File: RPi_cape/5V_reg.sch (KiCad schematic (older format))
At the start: 18 parts, among them U34 LMZ14203

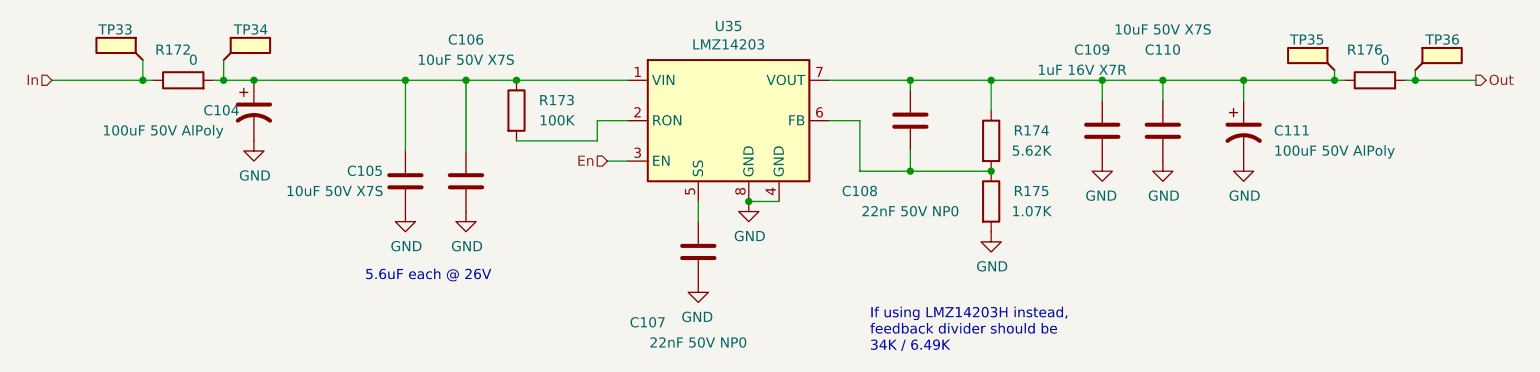
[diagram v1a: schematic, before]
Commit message: Updates based on testing, extra documentation
Added thermal calculations, possible thermal-induced problems to fault-condition list
Renamed error calculations file
Added some bringup tests
Changed 24V LED resistors (R20, R22) to 24.9K to consolidate BOM
Adjusted audio amp volume and filtering according to breadboard experiments
Moved bottom-end mounting holes and encoder connectors to avoid interfering mechanically with Raspberry Pi
Replaced under-sized power-ORing diodes with better Schottky option, added heatsinking with copper planes
Improved LMZ14203 heatsinking by removing thermal reliefs, re-arranging input-current-measurement testpoints to increase top-layer copper area
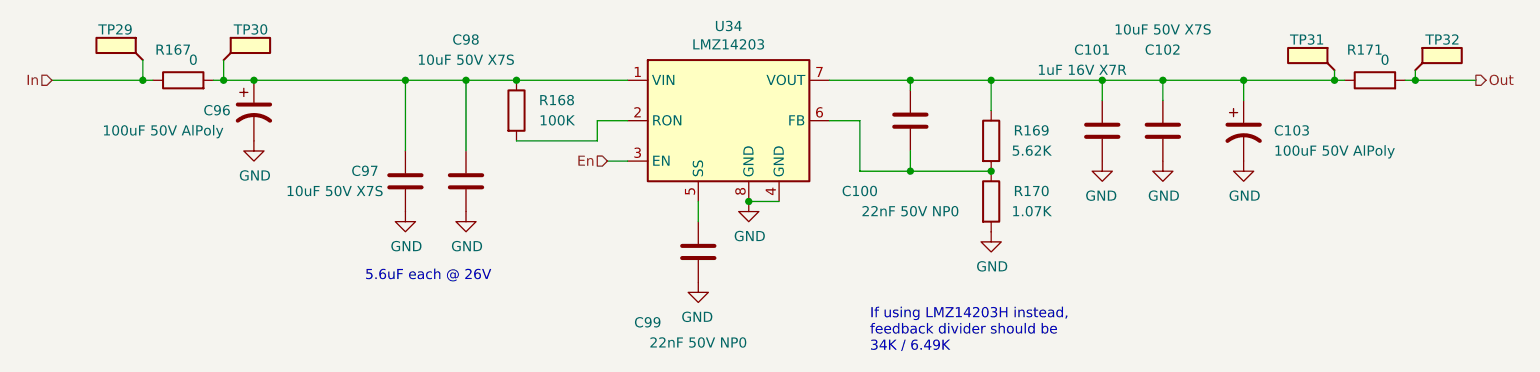
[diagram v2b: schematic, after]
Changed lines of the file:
@@
 $Descr A4 11693 8268
 encoding utf-8
-Sheet 11 15
+Sheet 10 15
 Title "Raspberry Pi Hat for JamVent Adaptation"
 Date ""
-Rev "1.8"
+Rev "1.9"
 Comp "US JamVent Team"
 Comment1 "Don Straney"
@@
 AR Path="/5EE065CD/5EE088D9" Ref="U34"  Part="1"
 AR Path="/5EEB3F52/5EE088D9" Ref="U35"  Part="1"
-F 0 "U35" H 5000 3417 50  0000 C CNN
+F 0 "U34" H 5000 3417 50  0000 C CNN
 F 1 "LMZ14203" H 5000 3326 50  0000 C CNN
 F 2 "Ventilator:TI_TO-PMOD-7" H 5000 2100 50  0001 C CNN
@@
 AR Path="/5EE065CD/5EE14EEB" Ref="R169"  Part="1"
 AR Path="/5EEB3F52/5EE14EEB" Ref="R174"  Part="1"
-F 0 "R174" H 6500 3100 50  0000 C CNN
+F 0 "R169" H 6500 3100 50  0000 C CNN
 F 1 "5.62K" H 6500 3000 50  0000 C CNN
 F 2 "Resistor_SMD:R_1206_3216Metric" V 6230 3050 50  0001 C CNN
@@
 AR Path="/5EE065CD/5EE14EF1" Ref="C97"  Part="1"
 AR Path="/5EEB3F52/5EE14EF1" Ref="C105"  Part="1"
-F 0 "C105" H 3600 3300 50  0000 C CNN
+F 0 "C97" H 3600 3300 50  0000 C CNN
 F 1 "10uF 50V X7S" H 3750 3200 50  0000 C CNN
 F 2 "Capacitor_SMD:C_1210_3225Metric" H 3438 3100 50  0001 C CNN
@@
 AR Path="/5EE065CD/5EE16CD0" Ref="R170"  Part="1"
 AR Path="/5EEB3F52/5EE16CD0" Ref="R175"  Part="1"
-F 0 "R175" H 6500 3400 50  0000 C CNN
+F 0 "R170" H 6500 3400 50  0000 C CNN
 F 1 "1.07K" H 6500 3300 50  0000 C CNN
 F 2 "Resistor_SMD:R_1206_3216Metric" V 6230 3350 50  0001 C CNN
@@
 AR Path="/5EE065CD/5EE170F2" Ref="R168"  Part="1"
 AR Path="/5EEB3F52/5EE170F2" Ref="R173"  Part="1"
-F 0 "R173" H 4150 2950 50  0000 C CNN
+F 0 "R168" H 4150 2950 50  0000 C CNN
 F 1 "100K" H 4150 2850 50  0000 C CNN
 F 2 "Resistor_SMD:R_1206_3216Metric" V 3880 2900 50  0001 C CNN
@@
 AR Path="/5EE065CD/5EE1CE10" Ref="#PWR0301"  Part="1"
 AR Path="/5EEB3F52/5EE1CE10" Ref="#PWR0310"  Part="1"
-F 0 "#PWR0310" H 3400 3150 50  0001 C CNN
+F 0 "#PWR0301" H 3400 3150 50  0001 C CNN
 F 1 "GND" H 3405 3227 50  0000 C CNN
 F 2 "" H 3400 3400 50  0001 C CNN
@@
 AR Path="/5EE065CD/5EE1D159" Ref="#PWR0304"  Part="1"
 AR Path="/5EEB3F52/5EE1D159" Ref="#PWR0313"  Part="1"
-F 0 "#PWR0313" H 5100 3100 50  0001 C CNN
+F 0 "#PWR0304" H 5100 3100 50  0001 C CNN
 F 1 "GND" H 5105 3177 50  0000 C CNN
 F 2 "" H 5100 3350 50  0001 C CNN
@@
 AR Path="/5EE065CD/5EE1E75C" Ref="#PWR0305"  Part="1"
 AR Path="/5EEB3F52/5EE1E75C" Ref="#PWR0314"  Part="1"
-F 0 "#PWR0314" H 6300 3250 50  0001 C CNN
+F 0 "#PWR0305" H 6300 3250 50  0001 C CNN
 F 1 "GND" H 6305 3327 50  0000 C CNN
 F 2 "" H 6300 3500 50  0001 C CNN
@@
 AR Path="/5EE065CD/5EE2670E" Ref="C99"  Part="1"
 AR Path="/5EEB3F52/5EE2670E" Ref="C107"  Part="1"
-F 0 "C107" H 4600 3950 50  0000 C CNN
+F 0 "C99" H 4600 3950 50  0000 C CNN
 F 1 "22nF 50V NP0" H 4850 4050 50  0000 C CNN
 F 2 "Capacitor_SMD:C_0805_2012Metric" H 4888 3450 50  0001 C CNN
@@
 AR Path="/5EE065CD/5EE26714" Ref="#PWR0303"  Part="1"
 AR Path="/5EEB3F52/5EE26714" Ref="#PWR0312"  Part="1"
-F 0 "#PWR0312" H 4850 3500 50  0001 C CNN
+F 0 "#PWR0303" H 4850 3500 50  0001 C CNN
 F 1 "GND" H 4855 3577 50  0000 C CNN
 F 2 "" H 4850 3750 50  0001 C CNN
@@
 AR Path="/5EE065CD/5EE27BE3" Ref="C100"  Part="1"
 AR Path="/5EEB3F52/5EE27BE3" Ref="C108"  Part="1"
-F 0 "C108" H 5650 3300 50  0000 C CNN
+F 0 "C100" H 5650 3300 50  0000 C CNN
 F 1 "22nF 50V NP0" H 5900 3400 50  0000 C CNN
 F 2 "Capacitor_SMD:C_0805_2012Metric" H 5938 2800 50  0001 C CNN
@@
 AR Path="/5EE065CD/5EE2ABB7" Ref="C102"  Part="1"
 AR Path="/5EEB3F52/5EE2ABB7" Ref="C110"  Part="1"
-F 0 "C110" H 7150 3400 50  0000 C CNN
+F 0 "C102" H 7150 3400 50  0000 C CNN
 F 1 "10uF 50V X7S" H 7150 3500 50  0000 C CNN
 F 2 "Capacitor_SMD:C_1210_3225Metric" H 7188 2850 50  0001 C CNN
@@
 AR Path="/5EE065CD/5EE2ABBD" Ref="#PWR0307"  Part="1"
 AR Path="/5EEB3F52/5EE2ABBD" Ref="#PWR0316"  Part="1"
-F 0 "#PWR0316" H 7150 2900 50  0001 C CNN
+F 0 "#PWR0307" H 7150 2900 50  0001 C CNN
 F 1 "GND" H 7155 2977 50  0000 C CNN
 F 2 "" H 7150 3150 50  0001 C CNN
@@
 AR Path="/5EE065CD/5EE35666" Ref="C96"  Part="1"
 AR Path="/5EEB3F52/5EE35666" Ref="C104"  Part="1"
-F 0 "C104" H 2400 2900 50  0000 L CNN
+F 0 "C96" H 2400 2900 50  0000 L CNN
 F 1 "100uF 50V AlPoly" H 1900 2800 50  0000 L CNN
 F 2 "Capacitor_SMD:CP_Elec_10x10.5" H 2650 2900 50  0001 C CNN
@@
 AR Path="/5EE065CD/5EE3566C" Ref="#PWR0300"  Part="1"
 AR Path="/5EEB3F52/5EE3566C" Ref="#PWR0309"  Part="1"
-F 0 "#PWR0309" H 2650 2800 50  0001 C CNN
+F 0 "#PWR0300" H 2650 2800 50  0001 C CNN
 F 1 "GND" H 2655 2877 50  0000 C CNN
 F 2 "" H 2650 3050 50  0001 C CNN
@@
 AR Path="/5EE065CD/5EE38A1F" Ref="C103"  Part="1"
 AR Path="/5EEB3F52/5EE38A1F" Ref="C111"  Part="1"
-F 0 "C111" H 7700 3000 50  0000 L CNN
+F 0 "C103" H 7700 3000 50  0000 L CNN
 F 1 "100uF 50V AlPoly" H 7700 2900 50  0000 L CNN
 F 2 "Capacitor_SMD:CP_Elec_10x10.5" H 7550 3000 50  0001 C CNN
@@
 AR Path="/5EE065CD/5EE38A25" Ref="#PWR0308"  Part="1"
 AR Path="/5EEB3F52/5EE38A25" Ref="#PWR0317"  Part="1"
-F 0 "#PWR0317" H 7550 2900 50  0001 C CNN
+F 0 "#PWR0308" H 7550 2900 50  0001 C CNN
 F 1 "GND" H 7555 2977 50  0000 C CNN
 F 2 "" H 7550 3150 50  0001 C CNN
@@
 AR Path="/5EE065CD/5EE41F5A" Ref="#PWR0306"  Part="1"
 AR Path="/5EEB3F52/5EE41F5A" Ref="#PWR0315"  Part="1"
-F 0 "#PWR0315" H 6850 2900 50  0001 C CNN
+F 0 "#PWR0306" H 6850 2900 50  0001 C CNN
 F 1 "GND" H 6855 2977 50  0000 C CNN
 F 2 "" H 6850 3150 50  0001 C CNN
@@
 AR Path="/5EE065CD/5EE41F60" Ref="C101"  Part="1"
 AR Path="/5EEB3F52/5EE41F60" Ref="C109"  Part="1"
-F 0 "C109" H 6800 2600 50  0000 C CNN
+F 0 "C101" H 6800 2600 50  0000 C CNN
 F 1 "1uF 16V X7R" H 6750 2700 50  0000 C CNN
 F 2 "Capacitor_SMD:C_0805_2012Metric" H 6888 2850 50  0001 C CNN
@@
 AR Path="/5EE065CD/5EE4C23D" Ref="R171"  Part="1"
 AR Path="/5EEB3F52/5EE4C23D" Ref="R176"  Part="1"
-F 0 "R176" V 8350 2800 50  0000 C CNN
+F 0 "R171" V 8350 2800 50  0000 C CNN
 F 1 "0" V 8300 2700 50  0000 C CNN
 F 2 "Resistor_SMD:R_1206_3216Metric" V 8130 2750 50  0001 C CNN
@@
 AR Path="/5EE065CD/5EE50890" Ref="R167"  Part="1"
 AR Path="/5EEB3F52/5EE50890" Ref="R172"  Part="1"
-F 0 "R172" V 2450 2800 50  0000 C CNN
+F 0 "R167" V 2450 2800 50  0000 C CNN
 F 1 "0" V 2400 2700 50  0000 C CNN
 F 2 "Resistor_SMD:R_1206_3216Metric" V 2230 2750 50  0001 C CNN
@@
 AR Path="/5EE065CD/5EEA6827" Ref="TP30"  Part="1"
 AR Path="/5EEB3F52/5EEA6827" Ref="TP34"  Part="1"
-F 0 "TP34" H 2550 2800 50  0000 L CNN
+F 0 "TP30" H 2550 2800 50  0000 L CNN
 F 1 "TestPoint_Flag" H 2760 2653 50  0001 L CNN
 F 2 "TestPoint:TestPoint_Keystone_5019_Minature" H 2700 2650 50  0001 C CNN
@@
 AR Path="/5EE065CD/5EEA7A58" Ref="TP29"  Part="1"
 AR Path="/5EEB3F52/5EEA7A58" Ref="TP33"  Part="1"
-F 0 "TP33" H 2150 2800 50  0000 L CNN
+F 0 "TP29" H 2150 2800 50  0000 L CNN
 F 1 "TestPoint_Flag" H 2360 2653 50  0001 L CNN
 F 2 "TestPoint:TestPoint_Keystone_5019_Minature" H 2300 2650 50  0001 C CNN
@@
 AR Path="/5EE065CD/5EEA8BCB" Ref="TP31"  Part="1"
 AR Path="/5EEB3F52/5EEA8BCB" Ref="TP35"  Part="1"
-F 0 "TP35" H 8050 2850 50  0000 L CNN
+F 0 "TP31" H 8050 2850 50  0000 L CNN
 F 1 "TestPoint_Flag" H 8260 2703 50  0001 L CNN
 F 2 "TestPoint:TestPoint_Keystone_5019_Minature" H 8200 2700 50  0001 C CNN
@@
 AR Path="/5EE065CD/5EEAED2A" Ref="TP32"  Part="1"
 AR Path="/5EEB3F52/5EEAED2A" Ref="TP36"  Part="1"
-F 0 "TP36" H 8450 2850 50  0000 L CNN
+F 0 "TP32" H 8450 2850 50  0000 L CNN
 F 1 "TestPoint_Flag" H 8660 2703 50  0001 L CNN
 F 2 "TestPoint:TestPoint_Keystone_5019_Minature" H 8600 2700 50  0001 C CNN
@@
 AR Path="/5EE065CD/5F025002" Ref="C98"  Part="1"
 AR Path="/5EEB3F52/5F025002" Ref="C106"  Part="1"
-F 0 "C106" H 3700 3950 50  0000 C CNN
+F 0 "C98" H 3700 3950 50  0000 C CNN
 F 1 "10uF 50V X7S" H 3700 3850 50  0000 C CNN
 F 2 "Capacitor_SMD:C_1210_3225Metric" H 3738 3100 50  0001 C CNN
@@
 AR Path="/5EE065CD/5F025009" Ref="#PWR0302"  Part="1"
 AR Path="/5EEB3F52/5F025009" Ref="#PWR0311"  Part="1"
-F 0 "#PWR0311" H 3700 3150 50  0001 C CNN
+F 0 "#PWR0302" H 3700 3150 50  0001 C CNN
 F 1 "GND" H 3705 3227 50  0000 C CNN
 F 2 "" H 3700 3400 50  0001 C CNN

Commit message: Cleanup, manufacturing
Added doc on differences between 'proto' version and 'full' version
Added manufacturing README in proto version
Removed unused hardwired-limited O2 alarm nets in proto version
Fixed missed-annotation on D1 in full version
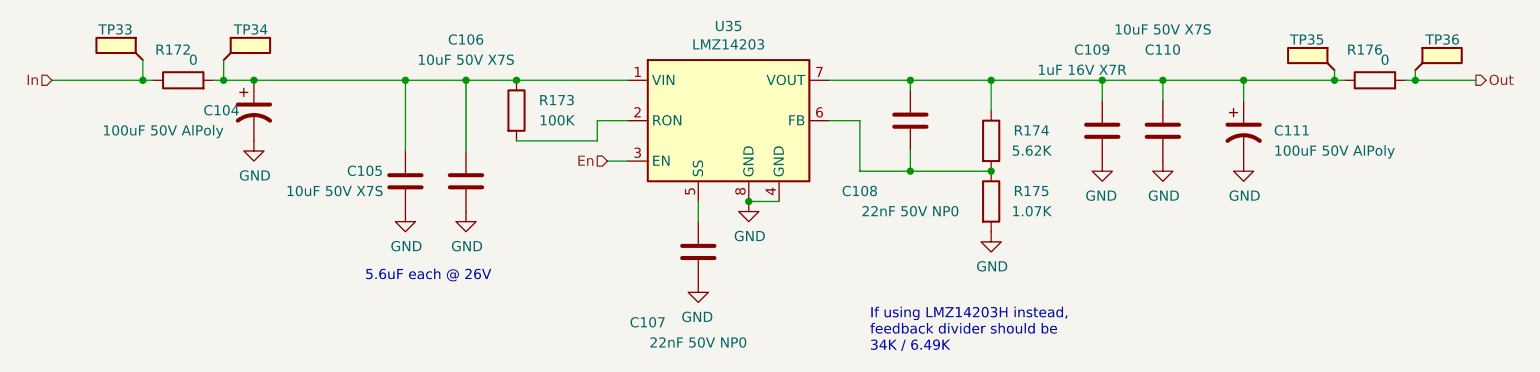
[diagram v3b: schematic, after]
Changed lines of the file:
@@
 $Descr A4 11693 8268
 encoding utf-8
-Sheet 10 15
+Sheet 11 15
 Title "Raspberry Pi Hat for JamVent Adaptation"
 Date ""
@@
 AR Path="/5EE065CD/5EE088D9" Ref="U34"  Part="1"
 AR Path="/5EEB3F52/5EE088D9" Ref="U35"  Part="1"
-F 0 "U34" H 5000 3417 50  0000 C CNN
+F 0 "U35" H 5000 3417 50  0000 C CNN
 F 1 "LMZ14203" H 5000 3326 50  0000 C CNN
 F 2 "Ventilator:TI_TO-PMOD-7" H 5000 2100 50  0001 C CNN
@@
 AR Path="/5EE065CD/5EE14EEB" Ref="R169"  Part="1"
 AR Path="/5EEB3F52/5EE14EEB" Ref="R174"  Part="1"
-F 0 "R169" H 6500 3100 50  0000 C CNN
+F 0 "R174" H 6500 3100 50  0000 C CNN
 F 1 "5.62K" H 6500 3000 50  0000 C CNN
 F 2 "Resistor_SMD:R_1206_3216Metric" V 6230 3050 50  0001 C CNN
@@
 AR Path="/5EE065CD/5EE14EF1" Ref="C97"  Part="1"
 AR Path="/5EEB3F52/5EE14EF1" Ref="C105"  Part="1"
-F 0 "C97" H 3600 3300 50  0000 C CNN
+F 0 "C105" H 3600 3300 50  0000 C CNN
 F 1 "10uF 50V X7S" H 3750 3200 50  0000 C CNN
 F 2 "Capacitor_SMD:C_1210_3225Metric" H 3438 3100 50  0001 C CNN
@@
 AR Path="/5EE065CD/5EE16CD0" Ref="R170"  Part="1"
 AR Path="/5EEB3F52/5EE16CD0" Ref="R175"  Part="1"
-F 0 "R170" H 6500 3400 50  0000 C CNN
+F 0 "R175" H 6500 3400 50  0000 C CNN
 F 1 "1.07K" H 6500 3300 50  0000 C CNN
 F 2 "Resistor_SMD:R_1206_3216Metric" V 6230 3350 50  0001 C CNN
@@
 AR Path="/5EE065CD/5EE170F2" Ref="R168"  Part="1"
 AR Path="/5EEB3F52/5EE170F2" Ref="R173"  Part="1"
-F 0 "R168" H 4150 2950 50  0000 C CNN
+F 0 "R173" H 4150 2950 50  0000 C CNN
 F 1 "100K" H 4150 2850 50  0000 C CNN
 F 2 "Resistor_SMD:R_1206_3216Metric" V 3880 2900 50  0001 C CNN
@@
 AR Path="/5EE065CD/5EE1CE10" Ref="#PWR0301"  Part="1"
 AR Path="/5EEB3F52/5EE1CE10" Ref="#PWR0310"  Part="1"
-F 0 "#PWR0301" H 3400 3150 50  0001 C CNN
+F 0 "#PWR0310" H 3400 3150 50  0001 C CNN
 F 1 "GND" H 3405 3227 50  0000 C CNN
 F 2 "" H 3400 3400 50  0001 C CNN
@@
 AR Path="/5EE065CD/5EE1D159" Ref="#PWR0304"  Part="1"
 AR Path="/5EEB3F52/5EE1D159" Ref="#PWR0313"  Part="1"
-F 0 "#PWR0304" H 5100 3100 50  0001 C CNN
+F 0 "#PWR0313" H 5100 3100 50  0001 C CNN
 F 1 "GND" H 5105 3177 50  0000 C CNN
 F 2 "" H 5100 3350 50  0001 C CNN
@@
 AR Path="/5EE065CD/5EE1E75C" Ref="#PWR0305"  Part="1"
 AR Path="/5EEB3F52/5EE1E75C" Ref="#PWR0314"  Part="1"
-F 0 "#PWR0305" H 6300 3250 50  0001 C CNN
+F 0 "#PWR0314" H 6300 3250 50  0001 C CNN
 F 1 "GND" H 6305 3327 50  0000 C CNN
 F 2 "" H 6300 3500 50  0001 C CNN
@@
 AR Path="/5EE065CD/5EE2670E" Ref="C99"  Part="1"
 AR Path="/5EEB3F52/5EE2670E" Ref="C107"  Part="1"
-F 0 "C99" H 4600 3950 50  0000 C CNN
+F 0 "C107" H 4600 3950 50  0000 C CNN
 F 1 "22nF 50V NP0" H 4850 4050 50  0000 C CNN
 F 2 "Capacitor_SMD:C_0805_2012Metric" H 4888 3450 50  0001 C CNN
@@
 AR Path="/5EE065CD/5EE26714" Ref="#PWR0303"  Part="1"
 AR Path="/5EEB3F52/5EE26714" Ref="#PWR0312"  Part="1"
-F 0 "#PWR0303" H 4850 3500 50  0001 C CNN
+F 0 "#PWR0312" H 4850 3500 50  0001 C CNN
 F 1 "GND" H 4855 3577 50  0000 C CNN
 F 2 "" H 4850 3750 50  0001 C CNN
@@
 AR Path="/5EE065CD/5EE27BE3" Ref="C100"  Part="1"
 AR Path="/5EEB3F52/5EE27BE3" Ref="C108"  Part="1"
-F 0 "C100" H 5650 3300 50  0000 C CNN
+F 0 "C108" H 5650 3300 50  0000 C CNN
 F 1 "22nF 50V NP0" H 5900 3400 50  0000 C CNN
 F 2 "Capacitor_SMD:C_0805_2012Metric" H 5938 2800 50  0001 C CNN
@@
 AR Path="/5EE065CD/5EE2ABB7" Ref="C102"  Part="1"
 AR Path="/5EEB3F52/5EE2ABB7" Ref="C110"  Part="1"
-F 0 "C102" H 7150 3400 50  0000 C CNN
+F 0 "C110" H 7150 3400 50  0000 C CNN
 F 1 "10uF 50V X7S" H 7150 3500 50  0000 C CNN
 F 2 "Capacitor_SMD:C_1210_3225Metric" H 7188 2850 50  0001 C CNN
@@
 AR Path="/5EE065CD/5EE2ABBD" Ref="#PWR0307"  Part="1"
 AR Path="/5EEB3F52/5EE2ABBD" Ref="#PWR0316"  Part="1"
-F 0 "#PWR0307" H 7150 2900 50  0001 C CNN
+F 0 "#PWR0316" H 7150 2900 50  0001 C CNN
 F 1 "GND" H 7155 2977 50  0000 C CNN
 F 2 "" H 7150 3150 50  0001 C CNN
@@
 AR Path="/5EE065CD/5EE35666" Ref="C96"  Part="1"
 AR Path="/5EEB3F52/5EE35666" Ref="C104"  Part="1"
-F 0 "C96" H 2400 2900 50  0000 L CNN
+F 0 "C104" H 2400 2900 50  0000 L CNN
 F 1 "100uF 50V AlPoly" H 1900 2800 50  0000 L CNN
 F 2 "Capacitor_SMD:CP_Elec_10x10.5" H 2650 2900 50  0001 C CNN
@@
 AR Path="/5EE065CD/5EE3566C" Ref="#PWR0300"  Part="1"
 AR Path="/5EEB3F52/5EE3566C" Ref="#PWR0309"  Part="1"
-F 0 "#PWR0300" H 2650 2800 50  0001 C CNN
+F 0 "#PWR0309" H 2650 2800 50  0001 C CNN
 F 1 "GND" H 2655 2877 50  0000 C CNN
 F 2 "" H 2650 3050 50  0001 C CNN
@@
 AR Path="/5EE065CD/5EE38A1F" Ref="C103"  Part="1"
 AR Path="/5EEB3F52/5EE38A1F" Ref="C111"  Part="1"
-F 0 "C103" H 7700 3000 50  0000 L CNN
+F 0 "C111" H 7700 3000 50  0000 L CNN
 F 1 "100uF 50V AlPoly" H 7700 2900 50  0000 L CNN
 F 2 "Capacitor_SMD:CP_Elec_10x10.5" H 7550 3000 50  0001 C CNN
@@
 AR Path="/5EE065CD/5EE38A25" Ref="#PWR0308"  Part="1"
 AR Path="/5EEB3F52/5EE38A25" Ref="#PWR0317"  Part="1"
-F 0 "#PWR0308" H 7550 2900 50  0001 C CNN
+F 0 "#PWR0317" H 7550 2900 50  0001 C CNN
 F 1 "GND" H 7555 2977 50  0000 C CNN
 F 2 "" H 7550 3150 50  0001 C CNN
@@
 AR Path="/5EE065CD/5EE41F5A" Ref="#PWR0306"  Part="1"
 AR Path="/5EEB3F52/5EE41F5A" Ref="#PWR0315"  Part="1"
-F 0 "#PWR0306" H 6850 2900 50  0001 C CNN
+F 0 "#PWR0315" H 6850 2900 50  0001 C CNN
 F 1 "GND" H 6855 2977 50  0000 C CNN
 F 2 "" H 6850 3150 50  0001 C CNN
@@
 AR Path="/5EE065CD/5EE41F60" Ref="C101"  Part="1"
 AR Path="/5EEB3F52/5EE41F60" Ref="C109"  Part="1"
-F 0 "C101" H 6800 2600 50  0000 C CNN
+F 0 "C109" H 6800 2600 50  0000 C CNN
 F 1 "1uF 16V X7R" H 6750 2700 50  0000 C CNN
 F 2 "Capacitor_SMD:C_0805_2012Metric" H 6888 2850 50  0001 C CNN
@@
 AR Path="/5EE065CD/5EE4C23D" Ref="R171"  Part="1"
 AR Path="/5EEB3F52/5EE4C23D" Ref="R176"  Part="1"
-F 0 "R171" V 8350 2800 50  0000 C CNN
+F 0 "R176" V 8350 2800 50  0000 C CNN
 F 1 "0" V 8300 2700 50  0000 C CNN
 F 2 "Resistor_SMD:R_1206_3216Metric" V 8130 2750 50  0001 C CNN
@@
 AR Path="/5EE065CD/5EE50890" Ref="R167"  Part="1"
 AR Path="/5EEB3F52/5EE50890" Ref="R172"  Part="1"
-F 0 "R167" V 2450 2800 50  0000 C CNN
+F 0 "R172" V 2450 2800 50  0000 C CNN
 F 1 "0" V 2400 2700 50  0000 C CNN
 F 2 "Resistor_SMD:R_1206_3216Metric" V 2230 2750 50  0001 C CNN
@@
 AR Path="/5EE065CD/5EEA6827" Ref="TP30"  Part="1"
 AR Path="/5EEB3F52/5EEA6827" Ref="TP34"  Part="1"
-F 0 "TP30" H 2550 2800 50  0000 L CNN
+F 0 "TP34" H 2550 2800 50  0000 L CNN
 F 1 "TestPoint_Flag" H 2760 2653 50  0001 L CNN
 F 2 "TestPoint:TestPoint_Keystone_5019_Minature" H 2700 2650 50  0001 C CNN
@@
 AR Path="/5EE065CD/5EEA7A58" Ref="TP29"  Part="1"
 AR Path="/5EEB3F52/5EEA7A58" Ref="TP33"  Part="1"
-F 0 "TP29" H 2150 2800 50  0000 L CNN
+F 0 "TP33" H 2150 2800 50  0000 L CNN
 F 1 "TestPoint_Flag" H 2360 2653 50  0001 L CNN
 F 2 "TestPoint:TestPoint_Keystone_5019_Minature" H 2300 2650 50  0001 C CNN
@@
 AR Path="/5EE065CD/5EEA8BCB" Ref="TP31"  Part="1"
 AR Path="/5EEB3F52/5EEA8BCB" Ref="TP35"  Part="1"
-F 0 "TP31" H 8050 2850 50  0000 L CNN
+F 0 "TP35" H 8050 2850 50  0000 L CNN
 F 1 "TestPoint_Flag" H 8260 2703 50  0001 L CNN
 F 2 "TestPoint:TestPoint_Keystone_5019_Minature" H 8200 2700 50  0001 C CNN
@@
 AR Path="/5EE065CD/5EEAED2A" Ref="TP32"  Part="1"
 AR Path="/5EEB3F52/5EEAED2A" Ref="TP36"  Part="1"
-F 0 "TP32" H 8450 2850 50  0000 L CNN
+F 0 "TP36" H 8450 2850 50  0000 L CNN
 F 1 "TestPoint_Flag" H 8660 2703 50  0001 L CNN
 F 2 "TestPoint:TestPoint_Keystone_5019_Minature" H 8600 2700 50  0001 C CNN
@@
 AR Path="/5EE065CD/5F025002" Ref="C98"  Part="1"
 AR Path="/5EEB3F52/5F025002" Ref="C106"  Part="1"
-F 0 "C98" H 3700 3950 50  0000 C CNN
+F 0 "C106" H 3700 3950 50  0000 C CNN
 F 1 "10uF 50V X7S" H 3700 3850 50  0000 C CNN
 F 2 "Capacitor_SMD:C_1210_3225Metric" H 3738 3100 50  0001 C CNN
@@
 AR Path="/5EE065CD/5F025009" Ref="#PWR0302"  Part="1"
 AR Path="/5EEB3F52/5F025009" Ref="#PWR0311"  Part="1"
-F 0 "#PWR0302" H 3700 3150 50  0001 C CNN
+F 0 "#PWR0311" H 3700 3150 50  0001 C CNN
 F 1 "GND" H 3705 3227 50  0000 C CNN
 F 2 "" H 3700 3400 50  0001 C CNN

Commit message: Admin (naming, license), improvements based on testing
Updated name on schematic, PCB silkscreen
Added 3 mounting holes on inside area of board for better mechanical robustness
Removed extra unused pressure sensor barb packages from library
Fixed Phoenix spring connector footprints, and added 3D models from Phoenix website
Added 3D models to TE encoder connector footprints, QFP-100 for CPLD, and 5019 testpoint
Changed DIAG_EN pin connection from valve drivers from +24V (too high) to +3.3V
Added CERN licensing terms
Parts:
- TP29, TP30, TP31, TP32: footprint TestPoint:TestPoint_Keystone_5019_Minature -> Ventilator:TestPoint_Keystone_5019_Minature
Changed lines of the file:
@@
 encoding utf-8
 Sheet 11 15
-Title "Raspberry Pi Hat for JamVent Adaptation"
+Title "GlobalVent Stand-Alone Controller"
 Date ""
-Rev "1.9"
-Comp "US JamVent Team"
-Comment1 "Don Straney"
-Comment2 ""
+Rev "1.10"
+Comp "US GlobalVent Team"
+Comment1 "Licensed under CERN-OHL-S v2"
+Comment2 "Don Straney"
 Comment3 ""
 Comment4 ""
@@
 F 0 "TP34" H 2550 2800 50  0000 L CNN
 F 1 "TestPoint_Flag" H 2760 2653 50  0001 L CNN
-F 2 "TestPoint:TestPoint_Keystone_5019_Minature" H 2700 2650 50  0001 C CNN
+F 2 "Ventilator:TestPoint_Keystone_5019_Minature" H 2700 2650 50  0001 C CNN
 F 3 "~" H 2700 2650 50  0001 C CNN
 F 4 "Keystone" H 2500 2650 50  0001 C CNN "Manufacturer"
@@
 F 0 "TP33" H 2150 2800 50  0000 L CNN
 F 1 "TestPoint_Flag" H 2360 2653 50  0001 L CNN
-F 2 "TestPoint:TestPoint_Keystone_5019_Minature" H 2300 2650 50  0001 C CNN
+F 2 "Ventilator:TestPoint_Keystone_5019_Minature" H 2300 2650 50  0001 C CNN
 F 3 "~" H 2300 2650 50  0001 C CNN
 F 4 "Keystone" H 2100 2650 50  0001 C CNN "Manufacturer"
@@
 F 0 "TP35" H 8050 2850 50  0000 L CNN
 F 1 "TestPoint_Flag" H 8260 2703 50  0001 L CNN
-F 2 "TestPoint:TestPoint_Keystone_5019_Minature" H 8200 2700 50  0001 C CNN
+F 2 "Ventilator:TestPoint_Keystone_5019_Minature" H 8200 2700 50  0001 C CNN
 F 3 "~" H 8200 2700 50  0001 C CNN
 F 4 "Keystone" H 8000 2700 50  0001 C CNN "Manufacturer"
@@
 F 0 "TP36" H 8450 2850 50  0000 L CNN
 F 1 "TestPoint_Flag" H 8660 2703 50  0001 L CNN
-F 2 "TestPoint:TestPoint_Keystone_5019_Minature" H 8600 2700 50  0001 C CNN
+F 2 "Ventilator:TestPoint_Keystone_5019_Minature" H 8600 2700 50  0001 C CNN
 F 3 "~" H 8600 2700 50  0001 C CNN
 F 4 "Keystone" H 8400 2700 50  0001 C CNN "Manufacturer"
